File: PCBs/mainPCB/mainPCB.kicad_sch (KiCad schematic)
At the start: 9 parts, among them SW1 RotaryEncoder_Switch, SW2 SW_Push, SW3 SW_Push, SW4 SW_Push

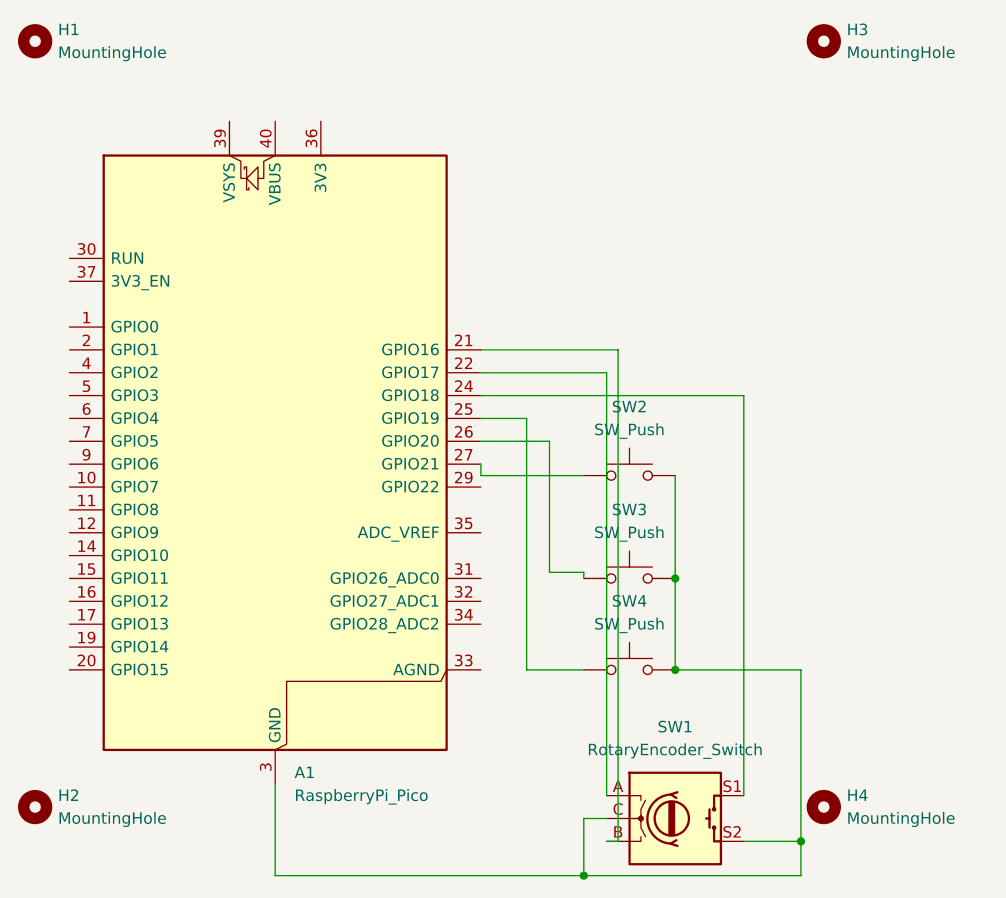
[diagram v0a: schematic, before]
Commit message: fixed PCB
retraced few traces, reworked rotary encoder to completely different design
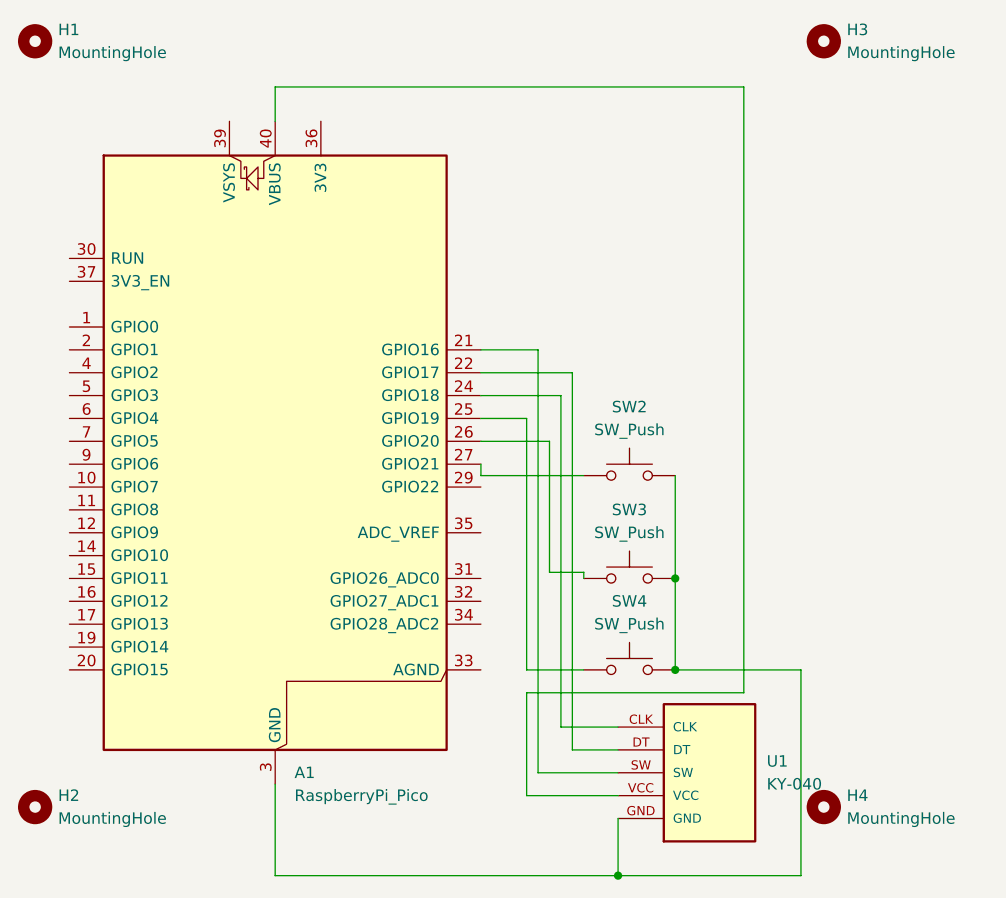
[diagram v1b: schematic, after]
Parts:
- removed SW1: RotaryEncoder_Switch, Rotary_Encoder:RotaryEncoder_Alps_EC11E-Switch_Vertical_H20mm_CircularMountingHoles, symbol Device:RotaryEncoder_Switch
- added U1: KY-040, KY-040:KY-040-PORT, symbol KY-040:KY-040
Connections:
- net at A1.22 (GPIO17): now also U1.DT
- net at A1.21 (GPIO16): now also U1.SW
- net at A1.13 (GND), A1.18 (GND), A1.23 (GND)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: now also U1.GND
- net at A1.24 (GPIO18): now also U1.CLK
- net at A1.40 (VBUS): now also U1.VCC
